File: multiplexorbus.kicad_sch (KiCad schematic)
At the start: 4 parts

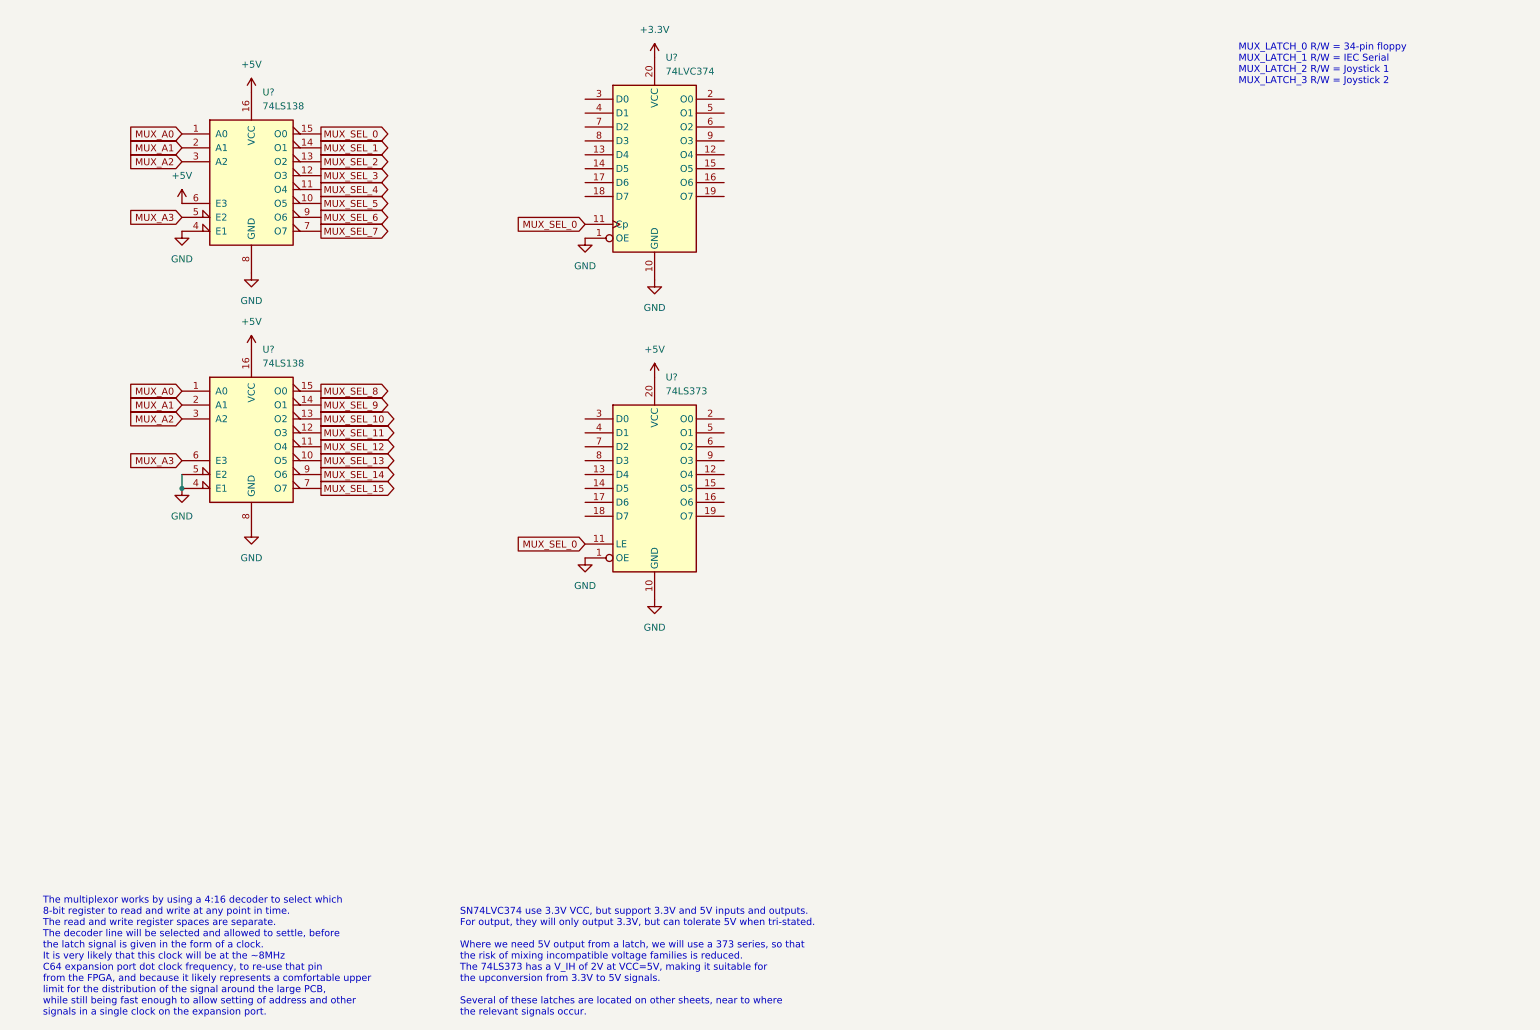
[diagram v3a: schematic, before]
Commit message: add inverting mux to allow use of 74LVC374 as tristate buffer
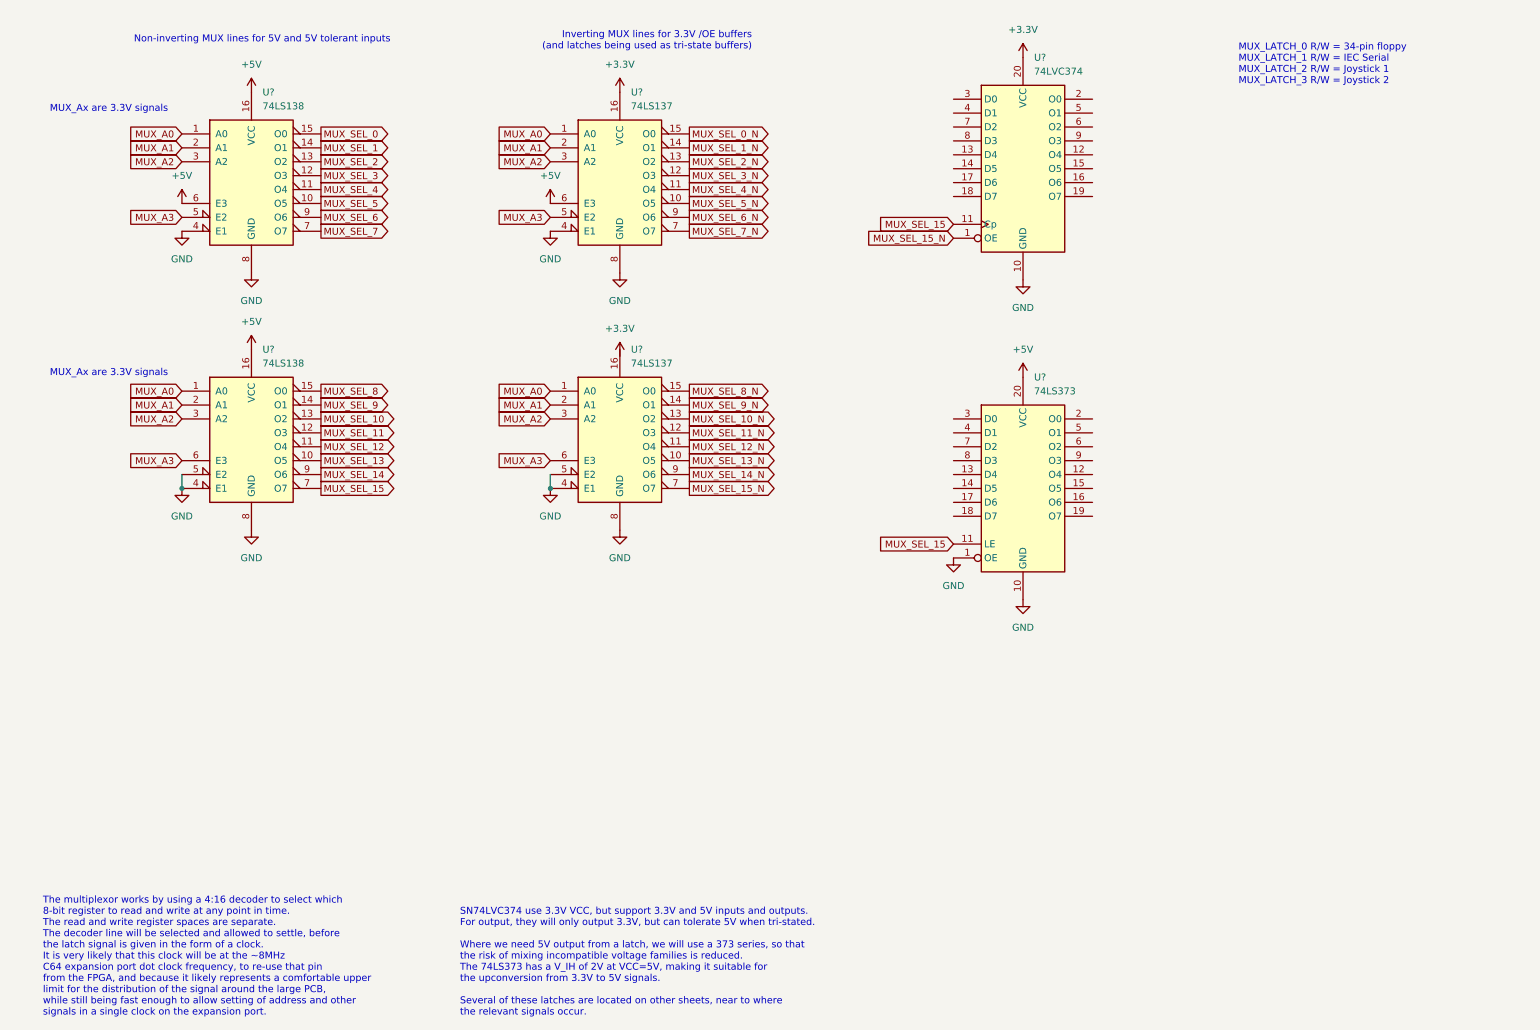
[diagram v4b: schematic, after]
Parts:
- added U? (x2): 74LS137, Package_DIP:DIP-16_W7.62mm, symbol 74xx:74LS138
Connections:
- net +3V3: now also U?.16 (VCC)
- net +5V: now also U?.6 (E3)
- net GND: now also U?.4 (E1), U?.4 (E1), U?.5 (E2), U?.8 (GND), U?.8 (GND); no longer U?.1 (OE)
- net MUX_A0: now also U?.1 (A0), U?.1 (A0)
- net MUX_A1: now also U?.2 (A1), U?.2 (A1)
- net MUX_A2: now also U?.3 (A2), U?.3 (A2)
- net MUX_A3: now also U?.5 (E2), U?.6 (E3)
- net MUX_SEL_0: no longer U?.11 (Cp), U?.11 (LE)
- net MUX_SEL_15: now also U?.11 (Cp), U?.11 (LE)
- new net MUX_SEL_0_N: U?.15 (O0)
- new net MUX_SEL_10_N: U?.13 (O2)
- new net MUX_SEL_11_N: U?.12 (O3)
- new net MUX_SEL_12_N: U?.11 (O4)
- new net MUX_SEL_13_N: U?.10 (O5)
- new net MUX_SEL_14_N: U?.9 (O6)
- new net MUX_SEL_15_N: U?.1 (OE), U?.7 (O7)
- new net MUX_SEL_1_N: U?.14 (O1)
- new net MUX_SEL_2_N: U?.13 (O2)
- new net MUX_SEL_3_N: U?.12 (O3)
- new net MUX_SEL_4_N: U?.11 (O4)
- new net MUX_SEL_5_N: U?.10 (O5)
- new net MUX_SEL_6_N: U?.9 (O6)
- new net MUX_SEL_7_N: U?.7 (O7)
- new net MUX_SEL_8_N: U?.15 (O0)
- new net MUX_SEL_9_N: U?.14 (O1)
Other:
- note added: "Inverting MUX lines for 3.3V /OE buffers (and latches being used as tri-state buffers)"
- note added: "MUX_Ax are 3.3V signals"
- note added: "Non-inverting MUX lines for 5V and 5V tolerant inputs"
- moved on the sheet: U?

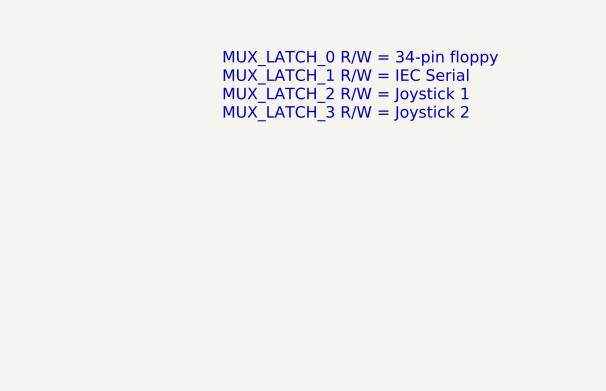
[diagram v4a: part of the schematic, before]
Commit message: begin implementing tape port. add symbols for C64 ports
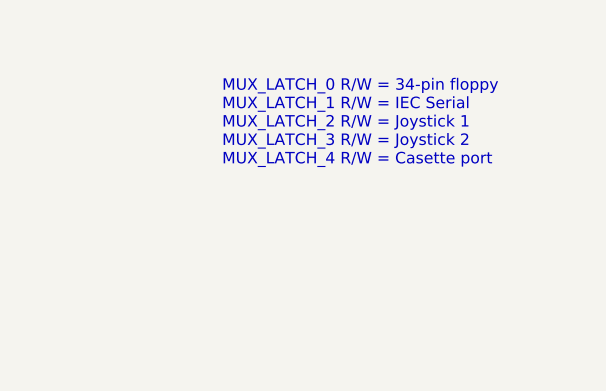
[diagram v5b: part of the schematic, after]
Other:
- note added: "MUX_LATCH_0 R/W = 34-pin floppy MUX_LATCH_1 R/W = IEC Serial MUX_LATCH_2 R/W = Joystick 1 MUX_LATCH_3 R/W = Joystick 2 MUX_LATCH_4 R/W = Casette port"
- note removed: "MUX_LATCH_0 R/W = 34-pin floppy MUX_LATCH_1 R/W = IEC Serial MUX_LATCH_2 R/W = Joystick 1 MUX_LATCH_3 R/W = Joystick 2"
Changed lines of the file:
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@@
     (effects (font (size 1.27 1.27)) (justify left bottom))
   )
-  (text "MUX_LATCH_0 R/W = 34-pin floppy\nMUX_LATCH_1 R/W = IEC Serial\nMUX_LATCH_2 R/W = Joystick 1\nMUX_LATCH_3 R/W = Joystick 2"
-    (at 233.68 24.13 0)
+  (text "MUX_LATCH_0 R/W = 34-pin floppy\nMUX_LATCH_1 R/W = IEC Serial\nMUX_LATCH_2 R/W = Joystick 1\nMUX_LATCH_3 R/W = Joystick 2\nMUX_LATCH_4 R/W = Casette port"
+    (at 233.68 29.21 0)
     (effects (font (size 1.27 1.27)) (justify left bottom))
   )

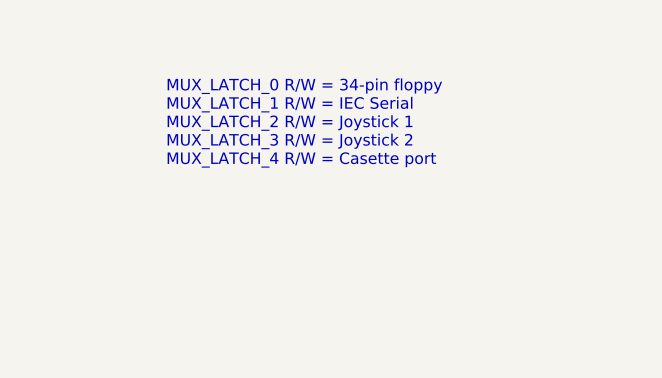
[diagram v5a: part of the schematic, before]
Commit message: create footprint for userport edge connector
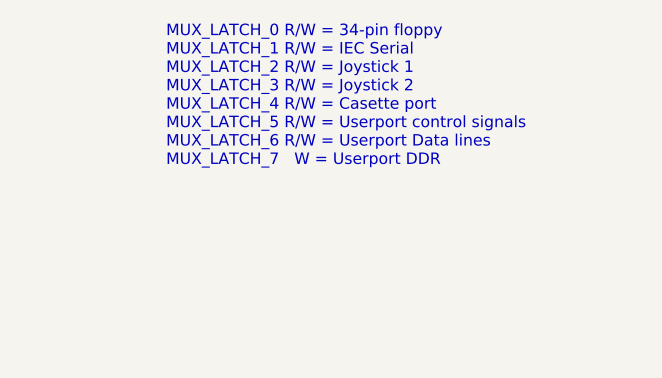
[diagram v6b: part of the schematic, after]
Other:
- note added: "MUX_LATCH_0 R/W = 34-pin floppy MUX_LATCH_1 R/W = IEC Serial MUX_LATCH_2 R/W = Joystick 1 MUX_LATCH_3 R/W = Joystick 2 MUX_LATCH_4 R/W = Casette port MUX_LATCH_5 R/W = Userport control signals MUX_LATCH_6 R/W = Userport Data lines MUX_LATCH_7 W = Userport DDR"
- note removed: "MUX_LATCH_0 R/W = 34-pin floppy MUX_LATCH_1 R/W = IEC Serial MUX_LATCH_2 R/W = Joystick 1 MUX_LATCH_3 R/W = Joystick 2 MUX_LATCH_4 R/W = Casette port"
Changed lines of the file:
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@@
     (effects (font (size 1.27 1.27)) (justify left bottom))
   )
-  (text "MUX_LATCH_0 R/W = 34-pin floppy\nMUX_LATCH_1 R/W = IEC Serial\nMUX_LATCH_2 R/W = Joystick 1\nMUX_LATCH_3 R/W = Joystick 2\nMUX_LATCH_4 R/W = Casette port"
+  (text "MUX_LATCH_0 R/W = 34-pin floppy\nMUX_LATCH_1 R/W = IEC Serial\nMUX_LATCH_2 R/W = Joystick 1\nMUX_LATCH_3 R/W = Joystick 2\nMUX_LATCH_4 R/W = Casette port\nMUX_LATCH_5 R/W = Userport control signals\nMUX_LATCH_6 R/W = Userport Data lines\nMUX_LATCH_7   W = Userport DDR"
     (at 233.68 29.21 0)
     (effects (font (size 1.27 1.27)) (justify left bottom))

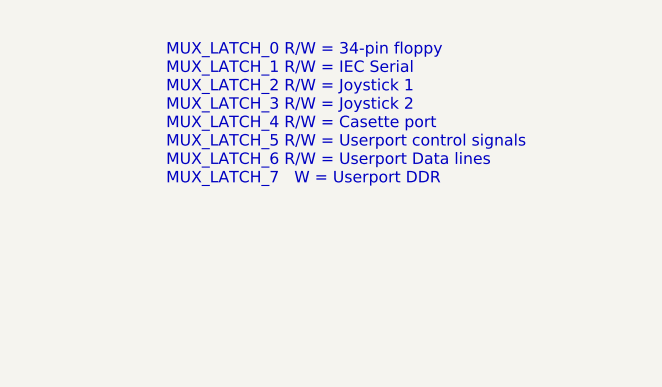
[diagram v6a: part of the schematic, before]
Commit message: add 8-way dipswitch bank
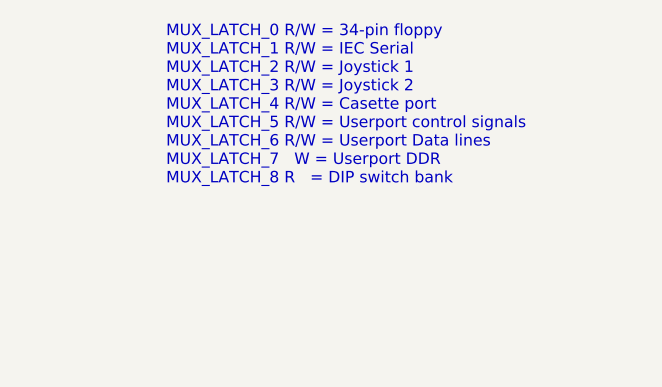
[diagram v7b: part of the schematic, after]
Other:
- note added: "MUX_LATCH_0 R/W = 34-pin floppy MUX_LATCH_1 R/W = IEC Serial MUX_LATCH_2 R/W = Joystick 1 MUX_LATCH_3 R/W = Joystick 2 MUX_LATCH_4 R/W = Casette port MUX_LATCH_5 R/W = Userport control signals MUX_LATCH_6 R/W = Userport Data lines MUX_LATCH_7 W = Userport DDR MUX_LATCH_8 R = DIP switch bank"
- note removed: "MUX_LATCH_0 R/W = 34-pin floppy MUX_LATCH_1 R/W = IEC Serial MUX_LATCH_2 R/W = Joystick 1 MUX_LATCH_3 R/W = Joystick 2 MUX_LATCH_4 R/W = Casette port MUX_LATCH_5 R/W = Userport control signals MUX_LATCH_6 R/W = Userport Data lines MUX_LATCH_7 W = Userport DDR"
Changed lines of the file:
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@@
     (effects (font (size 1.27 1.27)) (justify left bottom))
   )
-  (text "MUX_LATCH_0 R/W = 34-pin floppy\nMUX_LATCH_1 R/W = IEC Serial\nMUX_LATCH_2 R/W = Joystick 1\nMUX_LATCH_3 R/W = Joystick 2\nMUX_LATCH_4 R/W = Casette port\nMUX_LATCH_5 R/W = Userport control signals\nMUX_LATCH_6 R/W = Userport Data lines\nMUX_LATCH_7   W = Userport DDR"
+  (text "MUX_LATCH_0 R/W = 34-pin floppy\nMUX_LATCH_1 R/W = IEC Serial\nMUX_LATCH_2 R/W = Joystick 1\nMUX_LATCH_3 R/W = Joystick 2\nMUX_LATCH_4 R/W = Casette port\nMUX_LATCH_5 R/W = Userport control signals\nMUX_LATCH_6 R/W = Userport Data lines\nMUX_LATCH_7   W = Userport DDR\nMUX_LATCH_8 R   = DIP switch bank"
     (at 233.68 29.21 0)
     (effects (font (size 1.27 1.27)) (justify left bottom))
